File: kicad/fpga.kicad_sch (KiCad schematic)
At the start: 109 parts, among them Q4 BSS138LT1G, U1 XC7A100T-2FGG676I, X4 50MHz CMOS

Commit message: Step 2: bank 13 to 1.8V and the PSRAM move
SN74LXC8T245 datasheet SCES916A (rev. March 2023), section 6.3
Recommended Operating Conditions, page 5: VCCA 1.08 V to 5.5 V, so the
A side runs from +1V8_IO. Table 5-1 (page 3) states the same range on
the VCCA pin. Copy in ref/datasheets/sn74lxc8t245.pdf.

APS6404L-SQN-SN: datasheet rev 4.0, Table 9 page 26 (VDD 1.62 to 1.98 V,
ICC 7 mA), section 4.1 page 5 (SOP-8L(150): D 4.90, E1 3.90, E 6.00 BSC,
e 1.27 BSC), which the fitted SOIC-8_L4.9-W3.9-P1.27-LS6.0-BL matches.
Copy in ref/datasheets/aps6404l-sqn.pdf. The symbol for C5360304 is
imported into easyeda/EasyEDA.kicad_sym pointing at that footprint, and
load_pcb.py now refreshes the LCSC field on every sync.
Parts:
- added C394: 4.7uF, Capacitor_SMD:C_0603_1608Metric, symbol Device:C
- C370: value 100nF -> 47uF 6.3V; footprint Capacitor_SMD:C_0402_1005Metric -> Capacitor_SMD:C_1210_3225Metric; LCSC C1525 -> (none)
- C392: value 4.7uF -> 100nF; footprint Capacitor_SMD:C_0603_1608Metric -> Capacitor_SMD:C_0402_1005Metric; LCSC C277476 -> C1525
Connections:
- net +1V0_MGT: now also C380.1, C393.1; no longer C370.1, C392.1
- net +1V2_MGT: now also C392.1, C394.1; no longer C380.1, C393.1
- net +2V5: now also C369.1; no longer C368.1
- net +3V3: now also C367.1; no longer C330.1, C331.1, C332.1, C333.1, C334.1, C335.1, C366.1, U1.AC25 (VCCO_13), U1.T16 (VCCO_13), U1.T26 (VCCO_13), U1.U23 (VCCO_13), U1.V20 (VCCO_13), U1.Y24 (VCCO_13)
- net GND: now also C394.2
- net PSRAM0_CE_B: now also U1.T15 (IO_L20N_T3_13); no longer U1.M26 (IO_L20N_T3_A07_D23_14)
- net PSRAM0_IO0: now also U1.T17 (IO_L21P_T3_DQS_13); no longer U1.R26 (IO_L22P_T3_A05_D21_14)
- net PSRAM0_IO1: now also U1.T18 (IO_L21N_T3_DQS_13); no longer U1.P26 (IO_L22N_T3_A04_D20_14)
- net PSRAM0_IO2: now also U1.U15 (IO_L22P_T3_13); no longer U1.K25 (IO_L7P_T1_D09_14)
- net PSRAM0_IO3: now also U1.U16 (IO_L22N_T3_13); no longer U1.K26 (IO_L7N_T1_D10_14)
- net PSRAM0_SCK: now also U1.T14 (IO_L20P_T3_13); no longer U1.N26 (IO_L20P_T3_A08_D24_14)
- net PSRAM1_CE_B: now also U1.V14 (IO_L23N_T3_13); no longer U1.P25 (IO_L19N_T3_A09_D25_VREF_14)
- net PSRAM1_IO0: now also U1.V16 (IO_L24P_T3_13); no longer U1.L24 (IO_L9P_T1_DQS_14)
- net PSRAM1_IO1: now also U1.V17 (IO_L24N_T3_13); no longer U1.L25 (IO_L9N_T1_DQS_D13_14)
- net PSRAM1_IO2: now also U1.V18 (IO_L19P_T3_13); no longer U1.M24 (IO_L10P_T1_D14_14)
- net PSRAM1_IO3: now also U1.W18 (IO_L19N_T3_VREF_13); no longer U1.M25 (IO_L10N_T1_D15_14)
- net PSRAM1_SCK: now also U1.U14 (IO_L23P_T3_13); no longer U1.R25 (IO_L19P_T3_A10_D26_14)
- net PSRAM2_CE_B: now also U1.U19 (IO_L17N_T2_13); no longer U1.T25 (IO_L21N_T3_DQS_A06_D22_14)
- net PSRAM2_IO0: now also U1.V19 (IO_L18P_T2_13); no longer U1.N23 (IO_L15P_T2_DQS_RDWR_B_14)
- net PSRAM2_IO1: now also U1.W19 (IO_L18N_T2_13); no longer U1.N24 (IO_L15N_T2_DQS_DOUT_CSO_B_14)
- net PSRAM2_IO2: now also U1.T20 (IO_L15P_T2_DQS_13); no longer U1.P23 (IO_L17P_T2_A14_D30_14)
- net PSRAM2_IO3: now also U1.U20 (IO_L15N_T2_DQS_13); no longer U1.P24 (IO_L17N_T2_A13_D29_14)
- net PSRAM2_SCK: now also U1.T19 (IO_L17P_T2_13); no longer U1.T24 (IO_L21P_T3_DQS_14)
- net PSRAM3_CE_B: now also U1.Y20 (IO_L16N_T2_13); no longer U1.R23 (IO_L24N_T3_A00_D16_14)
- net PSRAM3_IO0: now also U1.W21 (IO_L14P_T2_SRCC_13); no longer U1.L22 (IO_L11P_T1_SRCC_14)
- net PSRAM3_IO1: now also U1.Y21 (IO_L14N_T2_SRCC_13); no longer U1.L23 (IO_L11N_T1_SRCC_14)
- net PSRAM3_IO2: now also U1.Y22 (IO_L11P_T1_SRCC_13); no longer U1.T22 (IO_L23P_T3_A03_D19_14)
- net PSRAM3_IO3: now also U1.Y23 (IO_L11N_T1_SRCC_13); no longer U1.R22 (IO_L23N_T3_A02_D18_14)
- net PSRAM3_SCK: now also U1.W20 (IO_L16P_T2_13); no longer U1.T23 (IO_L24P_T3_A01_D17_14)
- net VCCIO_1: now also C368.1; no longer C367.1
- net VCCIO_2: now also C370.1; no longer C369.1
- new net +1V8_IO: C330.1, C331.1, C332.1, C333.1, C334.1, C335.1, C366.1, U1.AC25 (VCCO_13), U1.T16 (VCCO_13), U1.T26 (VCCO_13), U1.U23 (VCCO_13), U1.V20 (VCCO_13), U1.Y24 (VCCO_13)
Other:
- note added: "Bulk capacitor shared by every FPGA I/O bank powered from +1V8_IO: UG483 Table 2-2 note 3 asks one 47 uF per group of up to four banks on one voltage. See ref/decoupling.md."
- note added: "decap VCCO group +1V8_IO"
- moved on the sheet: C246, C370, C371, C372, C373, C374, C375, C376, C377, C378, C379, C380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

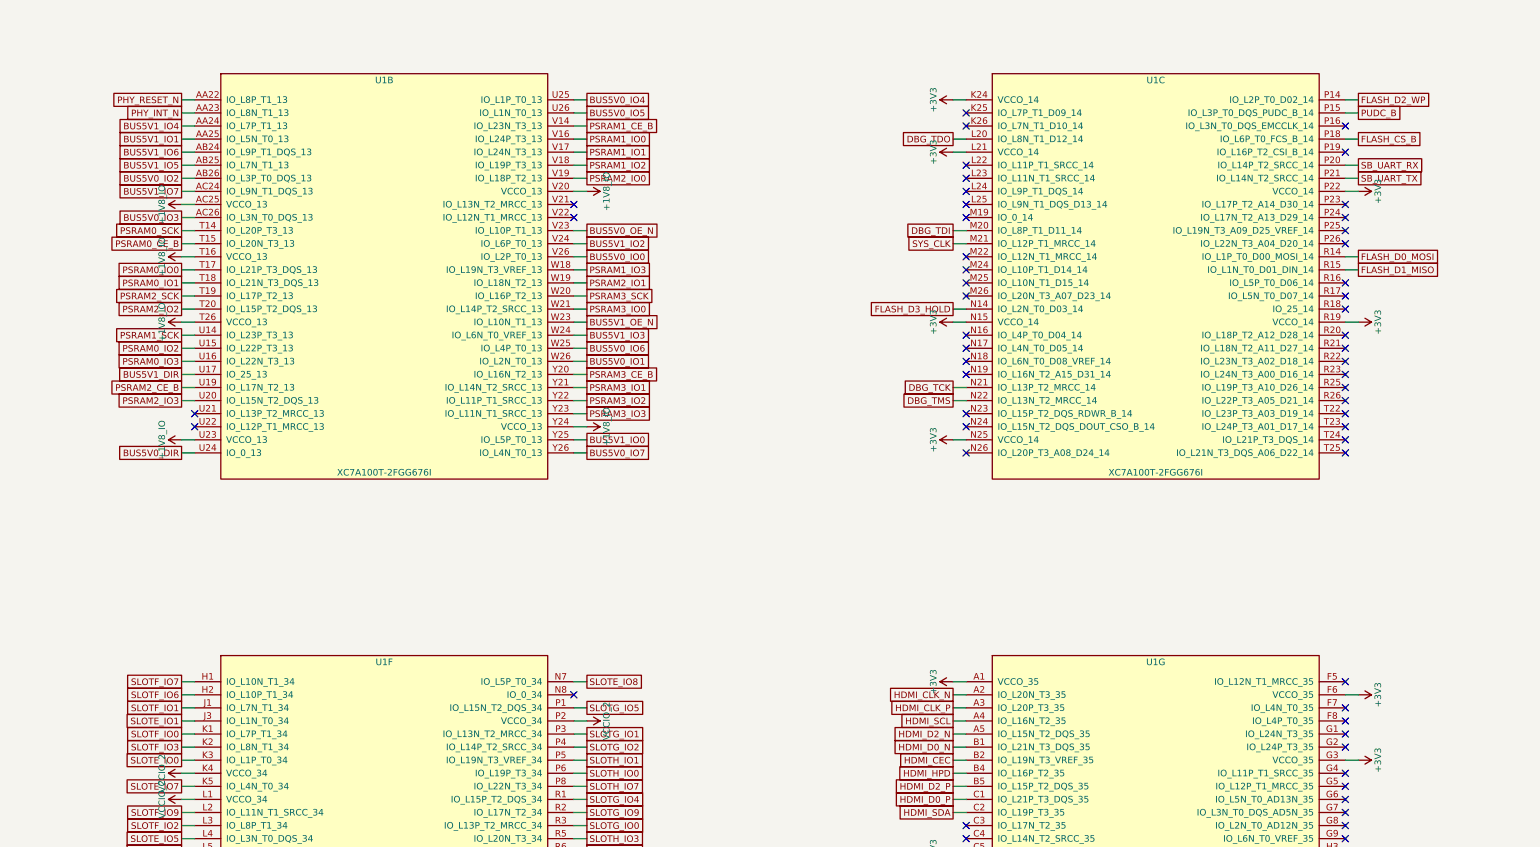
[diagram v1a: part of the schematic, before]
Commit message: Step 3: PHY control lines to bank 35
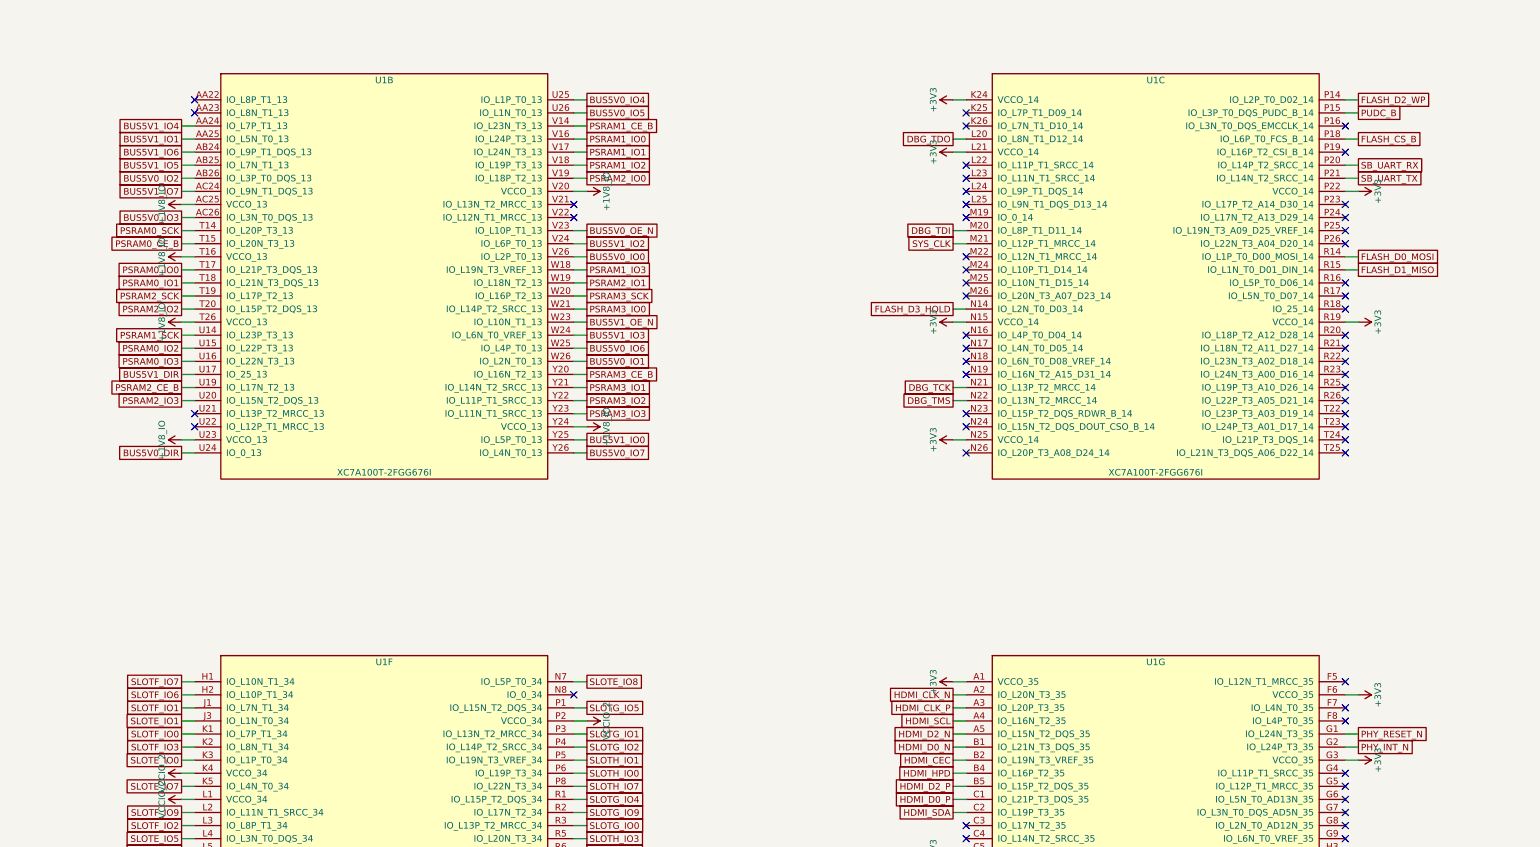
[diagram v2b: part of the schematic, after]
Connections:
- net PHY_INT_N: now also U1.G2 (IO_L24P_T3_35); no longer U1.AA23 (IO_L8N_T1_13)
- net PHY_RESET_N: now also U1.G1 (IO_L24N_T3_35); no longer U1.AA22 (IO_L8P_T1_13)
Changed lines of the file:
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@@
 		(instances (project "odin" (path "/c44fb7fe-6133-ad34-68fd-fb66126197ef/8cec9eb4-56b4-e78b-2213-febb3af15411" (reference "U1") (unit 2))))
 	)
-	(wire (pts (xy 226.06 78.74) (xy 223.52 78.74)) (stroke (width 0) (type default)))
-	(global_label "PHY_RESET_N" (shape passive) (at 223.52 78.74 0) (fields_autoplaced yes) (effects (font (size 1.27 1.27)) (justify right)))
-	(wire (pts (xy 226.06 81.28) (xy 223.52 81.28)) (stroke (width 0) (type default)))
-	(global_label "PHY_INT_N" (shape passive) (at 223.52 81.28 0) (fields_autoplaced yes) (effects (font (size 1.27 1.27)) (justify right)))
+	(no_connect (at 226.06 78.74))
+	(no_connect (at 226.06 81.28))
 	(wire (pts (xy 226.06 83.82) (xy 223.52 83.82)) (stroke (width 0) (type default)))
 	(global_label "BUS5V1_IO4" (shape passive) (at 223.52 83.82 0) (fields_autoplaced yes) (effects (font (size 1.27 1.27)) (justify right)))
@@
 	(no_connect (at 449.58 196.85))
 	(no_connect (at 449.58 199.39))
-	(no_connect (at 449.58 201.93))
-	(no_connect (at 449.58 204.47))
+	(wire (pts (xy 449.58 201.93) (xy 452.12 201.93)) (stroke (width 0) (type default)))
+	(global_label "PHY_RESET_N" (shape passive) (at 452.12 201.93 180) (fields_autoplaced yes) (effects (font (size 1.27 1.27)) (justify left)))
+	(wire (pts (xy 449.58 204.47) (xy 452.12 204.47)) (stroke (width 0) (type default)))
+	(global_label "PHY_INT_N" (shape passive) (at 452.12 204.47 180) (fields_autoplaced yes) (effects (font (size 1.27 1.27)) (justify left)))
 	(wire (pts (xy 449.58 207.01) (xy 452.12 207.01)) (stroke (width 0) (type default)))
 	(symbol (lib_id "power:+3V3") (at 452.12 207.01 270) (unit 1)

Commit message: Step 4: SDRAM
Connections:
- net SDRAM_RAS_N: now reaches U1.C3 (IO_L17N_T2_35)
- net SDRAM_CS_N: now reaches U1.D3 (IO_L17P_T2_35)
- net SDRAM_DQ1: now reaches U1.D6 (IO_L1N_T0_AD4N_35)
- net SDRAM_WE_N: now reaches U1.E3 (IO_L18N_T2_35)
- net SDRAM_DQ0: now reaches U1.E6 (IO_L1P_T0_AD4P_35)
- net SDRAM_CAS_N: now reaches U1.F3 (IO_L18P_T2_35)
- net SDRAM_DQ7: now reaches U1.F7 (IO_L4N_T0_35)
- net SDRAM_DQ6: now reaches U1.F8 (IO_L4P_T0_35)
- net SDRAM_DQ9: now reaches U1.G6 (IO_L5N_T0_AD13N_35)
- net SDRAM_DQ5: now reaches U1.G7 (IO_L3N_T0_DQS_AD5N_35)
- net SDRAM_DQ3: now reaches U1.G8 (IO_L2N_T0_AD12N_35)
- net SDRAM_DQ11: now reaches U1.G9 (IO_L6N_T0_VREF_35)
- net SDRAM_UDQM: now reaches U1.H4 (IO_L9N_T1_DQS_AD7N_35)
- net SDRAM_DQ8: now reaches U1.H6 (IO_L5P_T0_AD13P_35)
- net SDRAM_DQ4: now reaches U1.H7 (IO_L3P_T0_DQS_AD5P_35)
- net SDRAM_DQ2: now reaches U1.H8 (IO_L2P_T0_AD12P_35)
- net SDRAM_DQ10: now reaches U1.H9 (IO_L6P_T0_35)
- net SDRAM_LDQM: now reaches U1.J4 (IO_L9P_T1_DQS_AD7P_35)
- net SDRAM_DQ13: now reaches U1.J5 (IO_L7N_T1_AD6N_35)
- net SDRAM_DQ12: now reaches U1.J6 (IO_L7P_T1_AD6P_35)
- net SDRAM_CKE: now reaches U1.K6 (IO_L10N_T1_AD15N_35)
- net SDRAM_CLK: now reaches U1.K7 (IO_L10P_T1_AD15P_35)
- net SDRAM_DQ15: now reaches U1.K8 (IO_L8N_T1_AD14N_35)
- net SDRAM_DQ14: now reaches U1.L8 (IO_L8P_T1_AD14P_35)
- net SDRAM_A8: now reaches U1.M24 (IO_L10P_T1_D14_14)
- net SDRAM_A4: now reaches U1.M25 (IO_L10N_T1_D15_14)
- net SDRAM_A0: now reaches U1.M26 (IO_L20N_T3_A07_D23_14)
- net SDRAM_A12: now reaches U1.N23 (IO_L15P_T2_DQS_RDWR_B_14)
- net SDRAM_A9: now reaches U1.N24 (IO_L15N_T2_DQS_DOUT_CSO_B_14)
- net SDRAM_A1: now reaches U1.N26 (IO_L20P_T3_A08_D24_14)
- net SDRAM_BA0: now reaches U1.P23 (IO_L17P_T2_A14_D30_14)
- net SDRAM_A10: now reaches U1.P24 (IO_L17N_T2_A13_D29_14)
- net SDRAM_A5: now reaches U1.P25 (IO_L19N_T3_A09_D25_VREF_14)
- net SDRAM_A2: now reaches U1.P26 (IO_L22N_T3_A04_D20_14)
- net SDRAM_BA1: now reaches U1.R23 (IO_L24N_T3_A00_D16_14)
- net SDRAM_A6: now reaches U1.R25 (IO_L19P_T3_A10_D26_14)
- net SDRAM_A3: now reaches U1.R26 (IO_L22P_T3_A05_D21_14)
- net SDRAM_A11: now reaches U1.T24 (IO_L21P_T3_DQS_14)
- net SDRAM_A7: now reaches U1.T25 (IO_L21N_T3_DQS_A06_D22_14)
- no-connect marks 225 -> 186

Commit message: Step 5: MRAM, optional populate
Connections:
- net MRAM_CS: now reaches U1.K25 (IO_L7P_T1_D09_14)
- net MRAM_SCK: now reaches U1.K26 (IO_L7N_T1_D10_14)
- net MRAM_SI: now reaches U1.L24 (IO_L9P_T1_DQS_14)
- net MRAM_SO: now reaches U1.L25 (IO_L9N_T1_DQS_D13_14)
- no-connect marks 186 -> 182
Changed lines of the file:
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@@
 		(instances (project "odin" (path "/c44fb7fe-6133-ad34-68fd-fb66126197ef/8cec9eb4-56b4-e78b-2213-febb3af15411" (reference "#PWR0017") (unit 1))))
 	)
-	(no_connect (at 375.92 81.28))
-	(no_connect (at 375.92 83.82))
+	(wire (pts (xy 375.92 81.28) (xy 373.38 81.28)) (stroke (width 0) (type default)))
+	(global_label "MRAM_CS" (shape passive) (at 373.38 81.28 0) (fields_autoplaced yes) (effects (font (size 1.27 1.27)) (justify right)))
+	(wire (pts (xy 375.92 83.82) (xy 373.38 83.82)) (stroke (width 0) (type default)))
+	(global_label "MRAM_SCK" (shape passive) (at 373.38 83.82 0) (fields_autoplaced yes) (effects (font (size 1.27 1.27)) (justify right)))
 	(wire (pts (xy 375.92 86.36) (xy 373.38 86.36)) (stroke (width 0) (type default)))
 	(global_label "DBG_TDO" (shape passive) (at 373.38 86.36 0) (fields_autoplaced yes) (effects (font (size 1.27 1.27)) (justify right)))
@@
 	(no_connect (at 375.92 91.44))
 	(no_connect (at 375.92 93.98))
-	(no_connect (at 375.92 96.52))
-	(no_connect (at 375.92 99.06))
+	(wire (pts (xy 375.92 96.52) (xy 373.38 96.52)) (stroke (width 0) (type default)))
+	(global_label "MRAM_SI" (shape passive) (at 373.38 96.52 0) (fields_autoplaced yes) (effects (font (size 1.27 1.27)) (justify right)))
+	(wire (pts (xy 375.92 99.06) (xy 373.38 99.06)) (stroke (width 0) (type default)))
+	(global_label "MRAM_SO" (shape passive) (at 373.38 99.06 0) (fields_autoplaced yes) (effects (font (size 1.27 1.27)) (justify right)))
 	(no_connect (at 375.92 101.6))
 	(wire (pts (xy 375.92 104.14) (xy 373.38 104.14)) (stroke (width 0) (type default)))

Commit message: Step 6: microSD socket
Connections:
- net SD_CS: now reaches U1.L22 (IO_L11P_T1_SRCC_14)
- net SD_SCK: now reaches U1.L23 (IO_L11N_T1_SRCC_14)
- net SD_MISO: now reaches U1.R22 (IO_L23N_T3_A02_D18_14)
- net SD_MOSI: now reaches U1.T22 (IO_L23P_T3_A03_D19_14)
- net SD_CD: now reaches U1.T23 (IO_L24P_T3_A01_D17_14)
- no-connect marks 182 -> 177
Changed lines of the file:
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@@
 		(instances (project "odin" (path "/c44fb7fe-6133-ad34-68fd-fb66126197ef/8cec9eb4-56b4-e78b-2213-febb3af15411" (reference "#PWR0018") (unit 1))))
 	)
-	(no_connect (at 375.92 91.44))
-	(no_connect (at 375.92 93.98))
+	(wire (pts (xy 375.92 91.44) (xy 373.38 91.44)) (stroke (width 0) (type default)))
+	(global_label "SD_CS" (shape passive) (at 373.38 91.44 0) (fields_autoplaced yes) (effects (font (size 1.27 1.27)) (justify right)))
+	(wire (pts (xy 375.92 93.98) (xy 373.38 93.98)) (stroke (width 0) (type default)))
+	(global_label "SD_SCK" (shape passive) (at 373.38 93.98 0) (fields_autoplaced yes) (effects (font (size 1.27 1.27)) (justify right)))
 	(wire (pts (xy 375.92 96.52) (xy 373.38 96.52)) (stroke (width 0) (type default)))
 	(global_label "MRAM_SI" (shape passive) (at 373.38 96.52 0) (fields_autoplaced yes) (effects (font (size 1.27 1.27)) (justify right)))
@@
 	(no_connect (at 449.58 124.46))
 	(no_connect (at 449.58 127.0))
-	(no_connect (at 449.58 129.54))
+	(wire (pts (xy 449.58 129.54) (xy 452.12 129.54)) (stroke (width 0) (type default)))
+	(global_label "SD_MISO" (shape passive) (at 452.12 129.54 180) (fields_autoplaced yes) (effects (font (size 1.27 1.27)) (justify left)))
 	(wire (pts (xy 449.58 132.08) (xy 452.12 132.08)) (stroke (width 0) (type default)))
 	(global_label "SDRAM_BA1" (shape passive) (at 452.12 132.08 180) (fields_autoplaced yes) (effects (font (size 1.27 1.27)) (justify left)))
@@
 	(wire (pts (xy 449.58 137.16) (xy 452.12 137.16)) (stroke (width 0) (type default)))
 	(global_label "SDRAM_A3" (shape passive) (at 452.12 137.16 180) (fields_autoplaced yes) (effects (font (size 1.27 1.27)) (justify left)))
-	(no_connect (at 449.58 139.7))
-	(no_connect (at 449.58 142.24))
+	(wire (pts (xy 449.58 139.7) (xy 452.12 139.7)) (stroke (width 0) (type default)))
+	(global_label "SD_MOSI" (shape passive) (at 452.12 139.7 180) (fields_autoplaced yes) (effects (font (size 1.27 1.27)) (justify left)))
+	(wire (pts (xy 449.58 142.24) (xy 452.12 142.24)) (stroke (width 0) (type default)))
+	(global_label "SD_CD" (shape passive) (at 452.12 142.24 180) (fields_autoplaced yes) (effects (font (size 1.27 1.27)) (justify left)))
 	(wire (pts (xy 449.58 144.78) (xy 452.12 144.78)) (stroke (width 0) (type default)))
 	(global_label "SDRAM_A11" (shape passive) (at 452.12 144.78 180) (fields_autoplaced yes) (effects (font (size 1.27 1.27)) (justify left)))

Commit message: Step 7: regenerate and fix documents
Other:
- note added: "The FPGA is the board: every user design (a NEORV32 RISC-V core, a video pipeline, a protocol bridge) runs here. Its six user I/O banks are dedicated by job: bank 13 at 1.8 V carries the four PSRAMs and the two 5 V bus translators, bank 14 the configuration flash, the board-controller sideband, the 50 MHz clock, the SDRAM address bus, the MRAM and the microSD socket, banks 15 and 34 the direct ex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"
- note removed: "The FPGA is the board: every user design (a NEORV32 RISC-V core, a video pipeline, a protocol bridge) runs here. Its six user I/O banks are dedicated by job: bank 13 drives the two 5 V buses and the PHY reset/interrupt, bank 14 the PSRAM, the configuration flash, the board-controller sideband and the 50 MHz clock, banks 15 and 34 the direct extension slots A-D and E-H at a jumper-selected voltage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"
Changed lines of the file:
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@@
 	(rectangle (start 30.48 41.91) (end 646.43 521.97) (stroke (width 0.15) (type dash)) (fill (type none)))
 	(text "U1  FPGA" (at 33.02 45.72 0) (effects (font (size 2.2 2.2) (thickness 0.3)) (justify left)))
-	(text "The FPGA is the board: every user design (a NEORV32 RISC-V core, a video pipeline, a protocol bridge) runs here. Its six user I/O banks are dedicated by job: bank 13 drives the two 5 V buses and the PHY reset/interrupt, bank 14 the PSRAM, the configuration flash, the board-controller sideband and the 50 MHz clock, banks 15 and 34 the direct extension slots A-D and E-H at a jumper-selected voltage, bank 16 the network at 2.5\nV, bank 35 the HDMI output. Ball-by-ball list: ref/ballmap.md; constraints: ref/freya.xdc." (at 33.02 50.8 0) (effects (font (size 1.5 1.5) (italic yes)) (justify left top)))
+	(text "The FPGA is the board: every user design (a NEORV32 RISC-V core, a video pipeline, a protocol bridge) runs here. Its six user I/O banks are dedicated by job: bank 13 at 1.8 V carries the four PSRAMs and the two 5 V bus translators, bank 14 the configuration flash, the board-controller sideband, the 50 MHz clock, the SDRAM address bus, the MRAM and the microSD socket, banks 15 and 34 the direct extension slots A-D and E-H at\na jumper-selected voltage, bank 16 the network at 2.5 V, bank 35 the HDMI output, the SDRAM data bus and the PHY reset/interrupt. Ball-by-ball list: ref/ballmap.md; constraints: ref/freya.xdc." (at 33.02 50.8 0) (effects (font (size 1.5 1.5) (italic yes)) (justify left top)))
 	(rectangle (start 30.48 542.29) (end 543.56 603.25) (stroke (width 0.15) (type dash)) (fill (type none)))
 	(text "decap VCCINT" (at 33.02 546.1 0) (effects (font (size 2.2 2.2) (thickness 0.3)) (justify left)))

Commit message: Decoupling numbering: a new rail's 47uF appends; the sync keeps group membership
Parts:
- C370: value 47uF 6.3V -> 100nF; footprint Capacitor_SMD:C_1210_3225Metric -> Capacitor_SMD:C_0402_1005Metric; LCSC (none) -> C1525
- C392: value 100nF -> 4.7uF; footprint Capacitor_SMD:C_0402_1005Metric -> Capacitor_SMD:C_0603_1608Metric; LCSC C1525 -> C277476
- C394: value 4.7uF -> 47uF 6.3V; footprint Capacitor_SMD:C_0603_1608Metric -> Capacitor_SMD:C_1210_3225Metric; LCSC C277476 -> (none)
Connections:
- net +1V0_MGT: now also C370.1, C392.1; no longer C380.1, C393.1
- net +1V2_MGT: now also C380.1, C393.1; no longer C392.1, C394.1
- net +1V8_IO: now also C394.1; no longer C366.1
- net +2V5: now also C368.1; no longer C369.1
- net +3V3: now also C366.1; no longer C367.1
- net VCCIO_1: now also C367.1; no longer C368.1
- net VCCIO_2: now also C369.1; no longer C370.1
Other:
- moved on the sheet: C370, C371, C372, C373, C374, C375, C376, C377, C378, C379, C380, C381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
